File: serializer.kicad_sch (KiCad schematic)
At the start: 26 parts

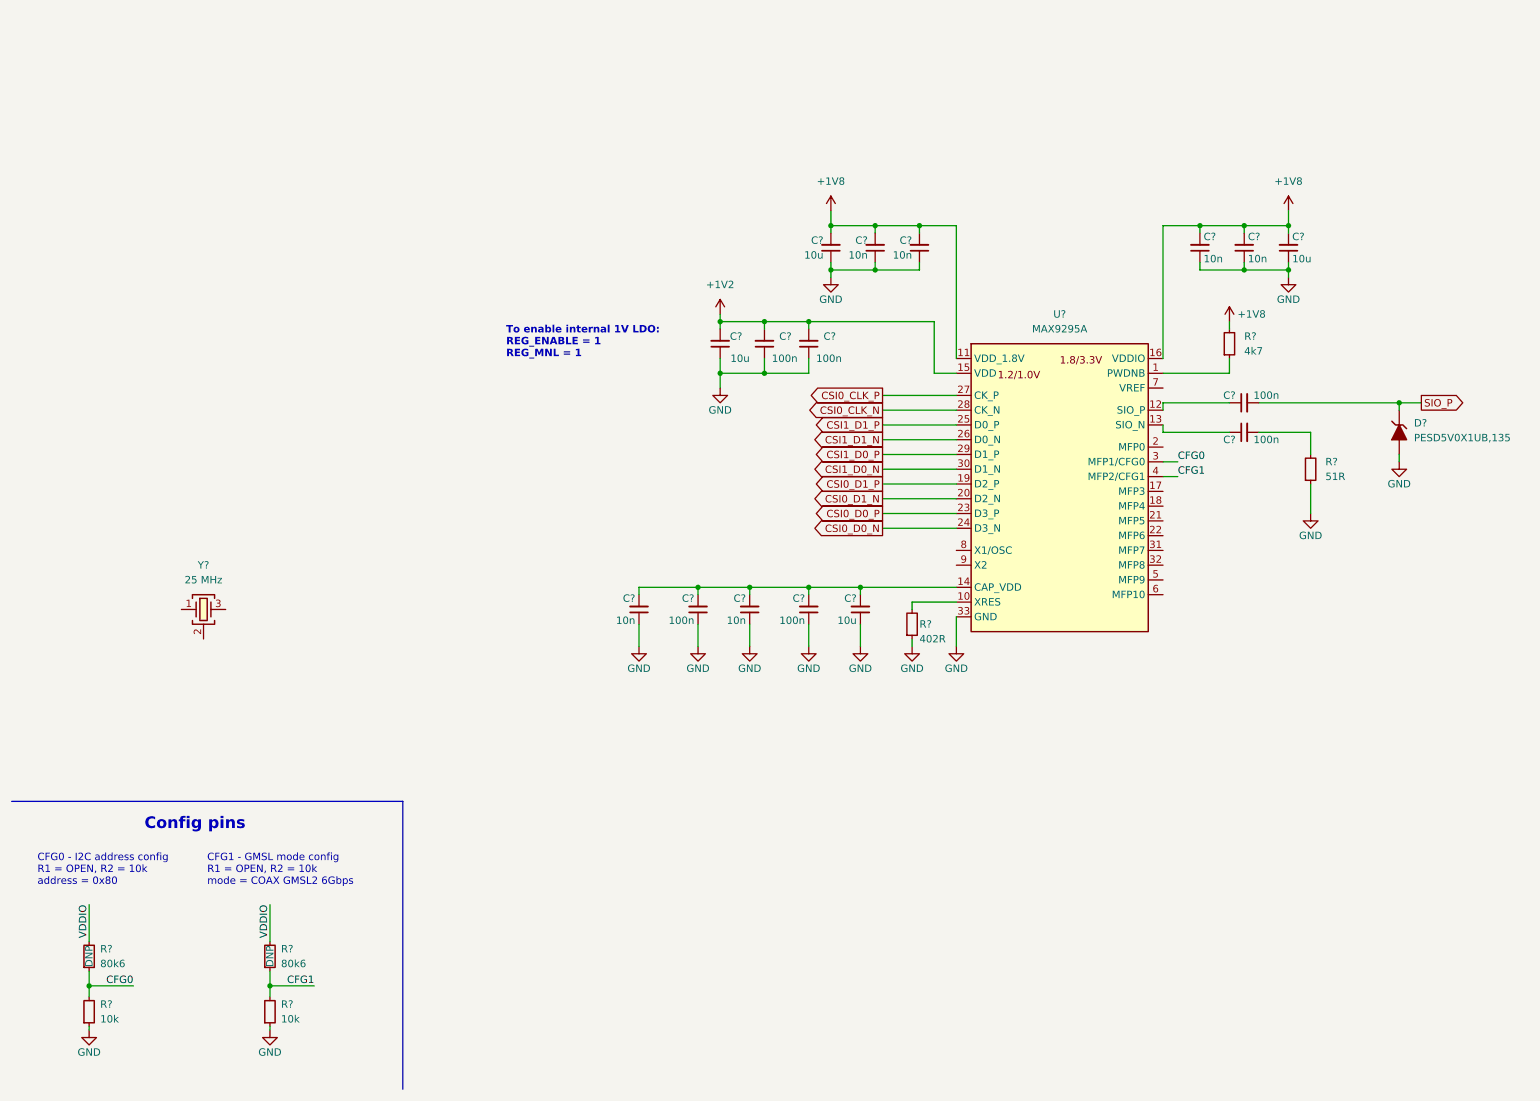
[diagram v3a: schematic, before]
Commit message: Add crystal to the serializer chip
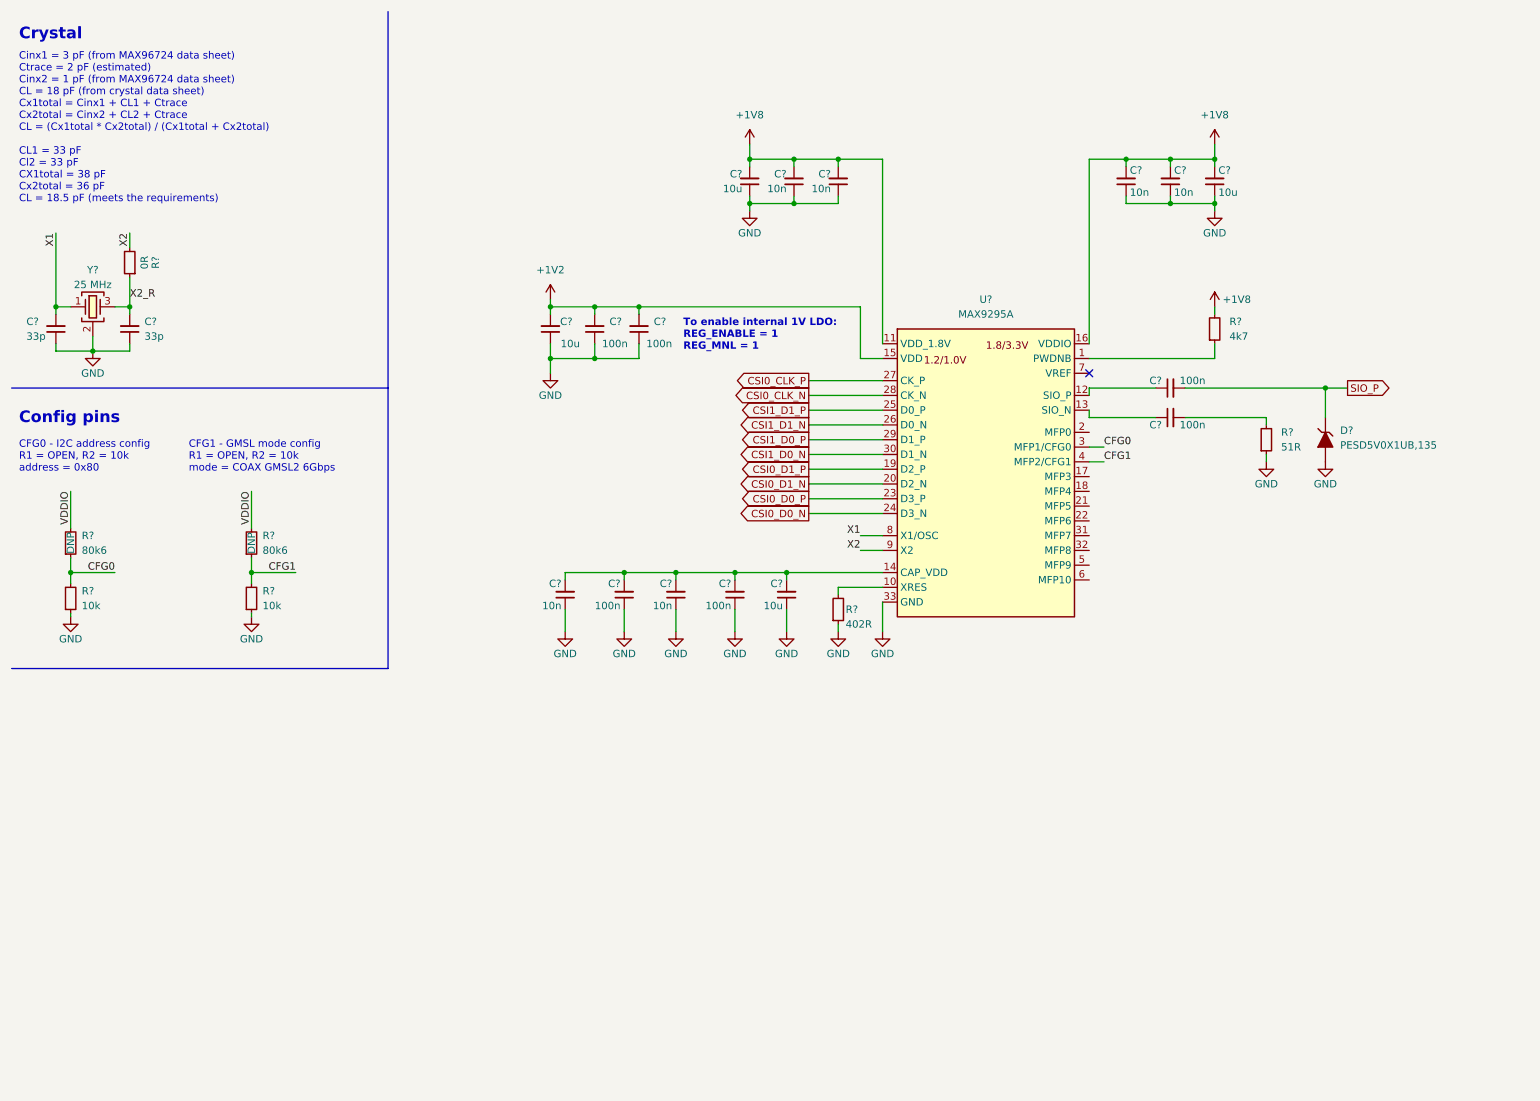
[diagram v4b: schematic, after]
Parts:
- removed Y?: Resonator_25MHz_ABM8G, antmicro-footprints:Oscillator_SMD_Geyer_KX-7-4Pin_3.2x2.5mm, symbol antmicroResonators:Resonator_25MHz_ABM8G
- added C? (x2): C_33p_0402, antmicro-footprints:C_0402_1005Metric, symbol antmicroCapacitors0402:C_33p_0402
- added R?: R_0R_0402, antmicro-footprints:R_0402_1005Metric, symbol antmicroResistors0402:R_0R_0402
- added Y?: Resonator_25MHz_ABM8G, antmicro-footprints:Oscillator_SMD_Geyer_KX-7-4Pin_3.2x2.5mm, symbol antmicroResonators:Resonator_25MHz_ABM8G
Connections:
- net GND: now also C?.1, C?.1, Y?.2 (SH), Y?.4 (SH)
- net X1: now reaches U?.8 (X1/OSC)
- net X1: now also C?.2, Y?.1
- net X2: now reaches U?.9 (X2)
- net X2: now also R?.2
- new net X2_R: C?.2, R?.1, Y?.3
- no-connect marks 0 -> 1
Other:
- note added: "Cinx1 = 3 pF (from MAX96724 data sheet) Ctrace = 2 pF (estimated) Cinx2 = 1 pF (from MAX96724 data sheet) CL = 18 pF (from crystal data sheet) Cx1total = Cinx1 + CL1 + Ctrace Cx2total = Cinx2 + CL2 + Ctrace CL = (Cx1total * Cx2total) / (Cx1total + Cx2total) CL1 = 33 pF Cl2 = 33 pF CX1total = 38 pF Cx2total = 36 pF CL = 18.5 pF (meets the requirements)"
- note added: "Crystal"
- moved on the sheet: C?, D?, R?, U?

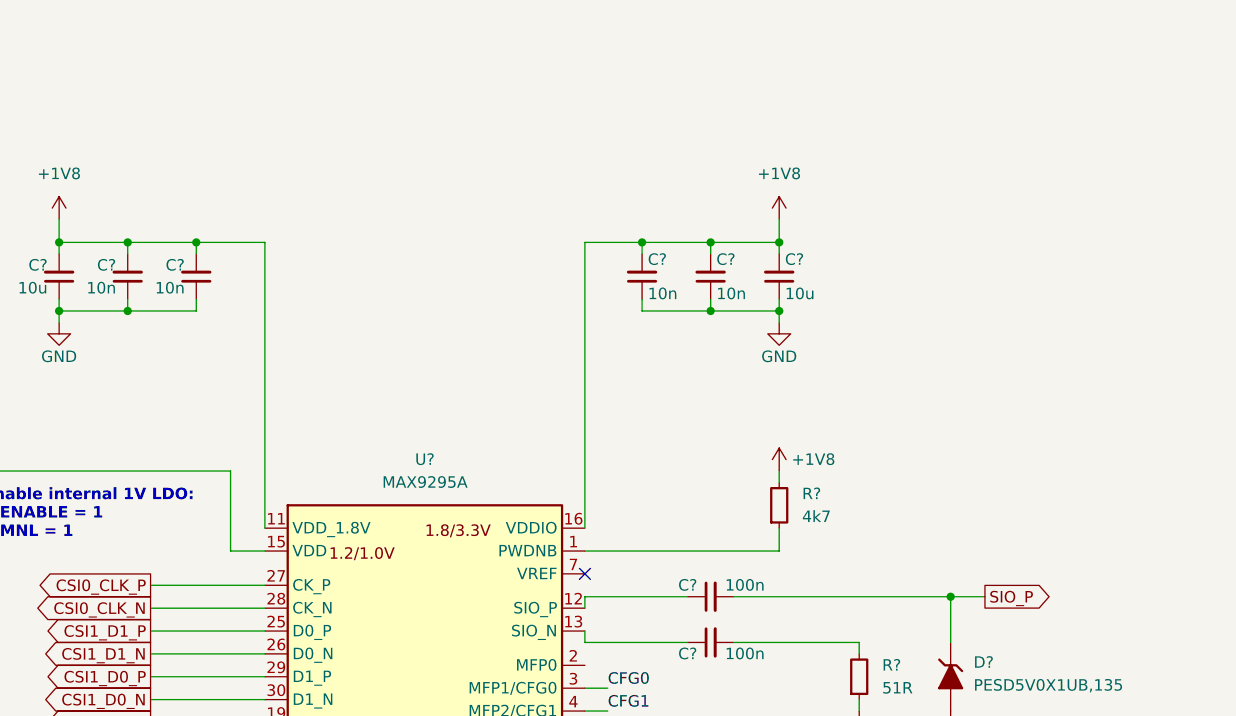
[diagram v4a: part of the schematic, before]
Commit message: Change VDDIO to 3V3
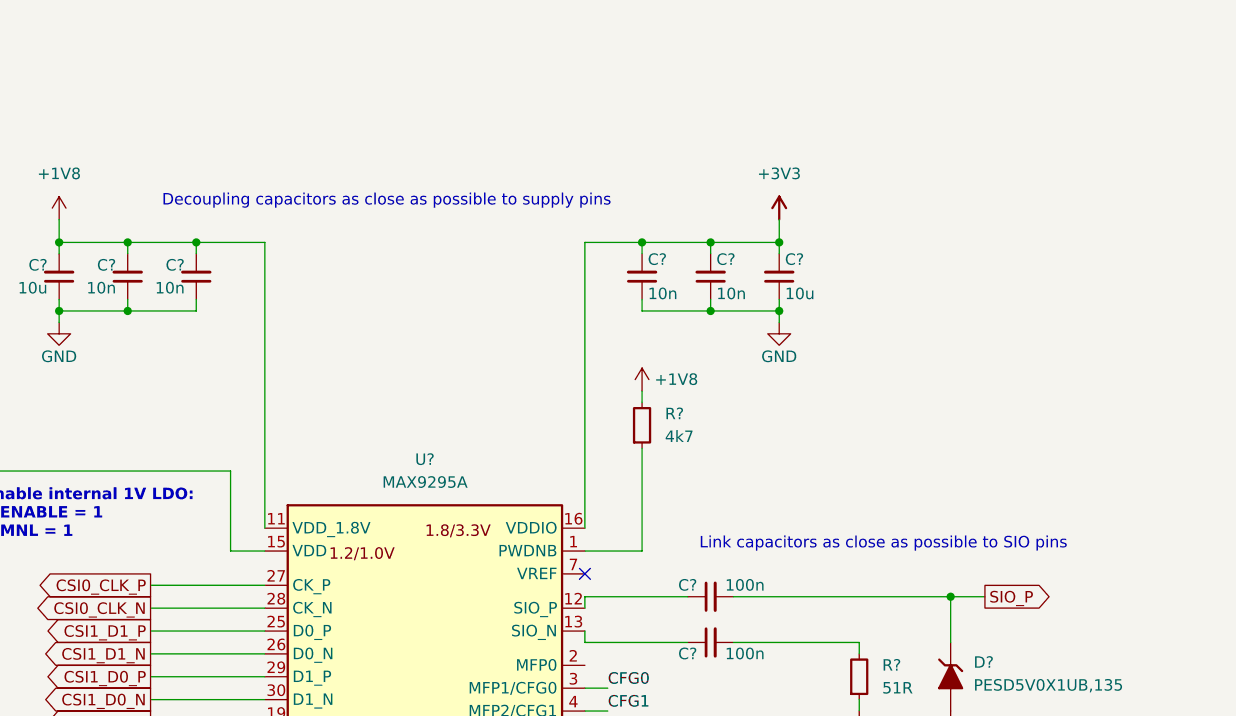
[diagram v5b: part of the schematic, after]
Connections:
- net +1V8: no longer C?.2, C?.2, C?.2, U?.16 (VDDIO)
- new net +3V3: C?.2, C?.2, C?.2, U?.16 (VDDIO)
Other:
- note added: "Decoupling capacitors as close as possible to supply pins"
- note added: "Link capacitors as close as possible to SIO pins"
- moved on the sheet: R?
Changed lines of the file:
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@@
     (stroke (width 0) (type default) (color 0 0 0 0))
   )
-  (wire (pts (xy 219.71 69.85) (xy 219.71 72.39))
+  (wire (pts (xy 204.47 60.96) (xy 204.47 72.39))
     (stroke (width 0) (type default) (color 0 0 0 0))
   )
@@
     (stroke (width 0) (type default) (color 0 0 0 0))
   )
+  (wire (pts (xy 198.12 72.39) (xy 204.47 72.39))
+    (stroke (width 0) (type default) (color 0 0 0 0))
+  )
   (wire (pts (xy 219.71 39.37) (xy 219.71 38.1))
     (stroke (width 0) (type default) (color 0 0 0 0))
@@
     (stroke (width 0) (type default) (color 0 0 0 0))
   )
-  (wire (pts (xy 219.71 63.5) (xy 219.71 64.77))
+  (wire (pts (xy 204.47 54.61) (xy 204.47 55.88))
     (stroke (width 0) (type default) (color 0 0 0 0))
   )
@@
   )
   (wire (pts (xy 198.12 69.85) (xy 198.12 38.1))
-    (stroke (width 0) (type default) (color 0 0 0 0))
-  )
-  (wire (pts (xy 198.12 72.39) (xy 219.71 72.39))
     (stroke (width 0) (type default) (color 0 0 0 0))
   )
@@
     (effects (font (size 1.27 1.27)) (justify left bottom))
   )
+  (text "Decoupling capacitors as close as possible to supply pins"
+    (at 151.13 34.29 0)
+    (effects (font (size 1.27 1.27)) (justify left bottom))
+  )
   (text "Cinx1 = 3 pF (from MAX96724 data sheet)\nCtrace = 2 pF (estimated)\nCinx2 = 1 pF (from MAX96724 data sheet)\nCL = 18 pF (from crystal data sheet)\nCx1total = Cinx1 + CL1 + Ctrace\nCx2total = Cinx2 + CL2 + Ctrace\nCL = (Cx1total * Cx2total) / (Cx1total + Cx2total)\n\nCL1 = 33 pF\nCl2 = 33 pF\nCX1total = 38 pF\nCx2total = 36 pF\nCL = 18.5 pF (meets the requirements)"
     (at 13.97 45.72 0)
@@
   (text "Config pins" (at 13.97 83.82 0)
     (effects (font (size 2 2) (thickness 0.4) bold) (justify left bottom))
+  )
+  (text "Link capacitors as close as possible to SIO pins" (at 210.82 72.39 0)
+    (effects (font (size 1.27 1.27)) (justify left bottom))
   )
   (label "X2" (at 158.75 105.41 180)
@@
     (pin "2")
   )
-  (symbol (lib_id "antmicropower:+1V8") (at 219.71 63.5 0) (unit 1)
-    (in_bom yes) (on_board yes)
-    (property "Reference" "#PWR?" (id 0) (at 234.95 66.04 0)
-      (effects (font (size 1.27 1.27) (thickness 0.15)) (justify left bottom) hide)
-    )
-    (property "Value" "+1V8" (id 1) (at 223.52 62.23 0)
-      (effects (font (size 1.27 1.27) (thickness 0.15)))
-    )
-    (property "Footprint" "" (id 2) (at 234.95 71.12 0)
-      (effects (font (size 1.27 1.27) (thickness 0.15)) (justify left bottom) hide)
-    )
-    (property "Datasheet" "" (id 3) (at 234.95 73.66 0)
-      (effects (font (size 1.27 1.27) (thickness 0.15)) (justify left bottom) hide)
-    )
-    (property "Author" "Antmicro" (id 4) (at 234.95 71.12 0)
-      (effects (font (size 1.27 1.27) (thickness 0.15)) (justify left bottom) hide)
-    )
-    (property "License" "Apache-2.0" (id 5) (at 234.95 73.66 0)
+  (symbol (lib_id "antmicropower:+1V8") (at 204.47 54.61 0) (unit 1)
+    (in_bom yes) (on_board yes)
+    (property "Reference" "#PWR?" (id 0) (at 219.71 57.15 0)
+      (effects (font (size 1.27 1.27) (thickness 0.15)) (justify left bottom) hide)
+    )
+    (property "Value" "+1V8" (id 1) (at 208.28 53.34 0)
+      (effects (font (size 1.27 1.27) (thickness 0.15)))
+    )
+    (property "Footprint" "" (id 2) (at 219.71 62.23 0)
+      (effects (font (size 1.27 1.27) (thickness 0.15)) (justify left bottom) hide)
+    )
+    (property "Datasheet" "" (id 3) (at 219.71 64.77 0)
+      (effects (font (size 1.27 1.27) (thickness 0.15)) (justify left bottom) hide)
+    )
+    (property "Author" "Antmicro" (id 4) (at 219.71 62.23 0)
+      (effects (font (size 1.27 1.27) (thickness 0.15)) (justify left bottom) hide)
+    )
+    (property "License" "Apache-2.0" (id 5) (at 219.71 64.77 0)
       (effects (font (size 1.27 1.27) (thickness 0.15)) (justify left bottom) hide)
     )
@@
     (pin "2")
   )
+  (symbol (lib_id "antmicropower:+3V3") (at 219.71 35.56 0) (unit 1)
+    (in_bom yes) (on_board yes) (fields_autoplaced)
+    (property "Reference" "#PWR?" (id 0) (at 234.95 38.1 0)
+      (effects (font (size 1.27 1.27) (thickness 0.15)) (justify left bottom) hide)
+    )
+    (property "Value" "+3V3" (id 1) (at 219.71 30.48 0)
+      (effects (font (size 1.27 1.27) (thickness 0.15)))
+    )
+    (property "Footprint" "" (id 2) (at 234.95 43.18 0)
+      (effects (font (size 1.27 1.27) (thickness 0.15)) (justify left bottom) hide)
+    )
+    (property "Datasheet" "" (id 3) (at 234.95 45.72 0)
+      (effects (font (size 1.27 1.27) (thickness 0.15)) (justify left bottom) hide)
+    )
+    (property "Author" "Antmicro" (id 4) (at 234.95 43.18 0)
+      (effects (font (size 1.27 1.27) (thickness 0.15)) (justify left bottom) hide)
+    )
+    (property "License" "Apache-2.0" (id 5) (at 234.95 45.72 0)
+      (effects (font (size 1.27 1.27) (thickness 0.15)) (justify left bottom) hide)
+    )
+    (pin "1")
+  )
   (symbol (lib_id "antmicroCapacitors0402:C_33p_0402") (at 33.02 69.85 90) (unit 1)
     (in_bom yes) (on_board yes)
@@
     (pin "2")
   )
-  (symbol (lib_id "antmicroResistors0402:R_4k7_0402") (at 219.71 69.85 90) (unit 1)
+  (symbol (lib_id "antmicroResistors0402:R_4k7_0402") (at 204.47 60.96 90) (unit 1)
     (in_bom yes) (on_board yes) (fields_autoplaced)
-    (property "Reference" "R?" (id 0) (at 222.25 66.0399 90)
-      (effects (font (size 1.27 1.27) (thickness 0.15)) (justify right))
-    )
-    (property "Value" "R_4k7_0402" (id 1) (at 232.41 49.53 0)
-      (effects (font (size 1.27 1.27) (thickness 0.15)) (justify left bottom) hide)
-    )
-    (property "Footprint" "antmicro-footprints:R_0402_1005Metric" (id 2) (at 234.95 49.53 0)
-      (effects (font (size 1.27 1.27) (thickness 0.15)) (justify left bottom) hide)
-    )
-    (property "Datasheet" "https://www.bourns.com/docs/product-datasheets/cr.pdf" (id 3) (at 237.49 49.53 0)
-      (effects (font (size 1.27 1.27) (thickness 0.15)) (justify left bottom) hide)
-    )
-    (property "MPN" "CR0402-FX-4701GLF" (id 4) (at 240.03 49.53 0)
-      (effects (font (size 1.27 1.27) (thickness 0.15)) (justify left bottom) hide)
-    )
-    (property "Manufacturer" "Bourns" (id 5) (at 242.57 49.53 0)
-      (effects (font (size 1.27 1.27) (thickness 0.15)) (justify left bottom) hide)
-    )
-    (property "License" "Apache-2.0" (id 6) (at 245.11 49.53 0)
-      (effects (font (size 1.27 1.27) (thickness 0.15)) (justify left bottom) hide)
-    )
-    (property "Author" "Antmicro" (id 7) (at 247.65 49.53 0)
-      (effects (font (size 1.27 1.27) (thickness 0.15)) (justify left bottom) hide)
-    )
-    (property "Val" "4k7" (id 8) (at 222.25 68.5799 90)
-      (effects (font (size 1.27 1.27) (thickness 0.15)) (justify right))
-    )
-    (property "Tolerance" "1%" (id 9) (at 229.87 49.53 0)
+    (property "Reference" "R?" (id 0) (at 207.01 57.1499 90)
+      (effects (font (size 1.27 1.27) (thickness 0.15)) (justify right))
+    )
+    (property "Value" "R_4k7_0402" (id 1) (at 217.17 40.64 0)
+      (effects (font (size 1.27 1.27) (thickness 0.15)) (justify left bottom) hide)
+    )
+    (property "Footprint" "antmicro-footprints:R_0402_1005Metric" (id 2) (at 219.71 40.64 0)
+      (effects (font (size 1.27 1.27) (thickness 0.15)) (justify left bottom) hide)
+    )
+    (property "Datasheet" "https://www.bourns.com/docs/product-datasheets/cr.pdf" (id 3) (at 222.25 40.64 0)
+      (effects (font (size 1.27 1.27) (thickness 0.15)) (justify left bottom) hide)
+    )
+    (property "MPN" "CR0402-FX-4701GLF" (id 4) (at 224.79 40.64 0)
+      (effects (font (size 1.27 1.27) (thickness 0.15)) (justify left bottom) hide)
+    )
+    (property "Manufacturer" "Bourns" (id 5) (at 227.33 40.64 0)
+      (effects (font (size 1.27 1.27) (thickness 0.15)) (justify left bottom) hide)
+    )
+    (property "License" "Apache-2.0" (id 6) (at 229.87 40.64 0)
+      (effects (font (size 1.27 1.27) (thickness 0.15)) (justify left bottom) hide)
+    )
+    (property "Author" "Antmicro" (id 7) (at 232.41 40.64 0)
+      (effects (font (size 1.27 1.27) (thickness 0.15)) (justify left bottom) hide)
+    )
+    (property "Val" "4k7" (id 8) (at 207.01 59.6899 90)
+      (effects (font (size 1.27 1.27) (thickness 0.15)) (justify right))
+    )
+    (property "Tolerance" "1%" (id 9) (at 214.63 40.64 0)
       (effects (font (size 1.27 1.27)) (justify left bottom) hide)
     )
@@
     (pin "2")
   )
-  (symbol (lib_id "antmicropower:+1V8") (at 219.71 35.56 0) (unit 1)
-    (in_bom yes) (on_board yes) (fields_autoplaced)
-    (property "Reference" "#PWR?" (id 0) (at 234.95 38.1 0)
-      (effects (font (size 1.27 1.27) (thickness 0.15)) (justify left bottom) hide)
-    )
-    (property "Value" "+1V8" (id 1) (at 219.71 30.48 0)
-      (effects (font (size 1.27 1.27) (thickness 0.15)))
-    )
-    (property "Footprint" "" (id 2) (at 234.95 43.18 0)
-      (effects (font (size 1.27 1.27) (thickness 0.15)) (justify left bottom) hide)
-    )
-    (property "Datasheet" "" (id 3) (at 234.95 45.72 0)
-      (effects (font (size 1.27 1.27) (thickness 0.15)) (justify left bottom) hide)
-    )
-    (property "Author" "Antmicro" (id 4) (at 234.95 43.18 0)
-      (effects (font (size 1.27 1.27) (thickness 0.15)) (justify left bottom) hide)
-    )
-    (property "License" "Apache-2.0" (id 5) (at 234.95 45.72 0)
-      (effects (font (size 1.27 1.27) (thickness 0.15)) (justify left bottom) hide)
-    )
-    (pin "1")
-  )
   (symbol (lib_id "antmicroCapacitors0402:C_100n_0402") (at 113.03 69.85 90) (unit 1)
